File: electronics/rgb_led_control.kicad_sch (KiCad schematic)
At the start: 7 parts, among them J1 rgb_led_conn, Q3 N-MOS, Q4 N-MOS, Q5 N-MOS

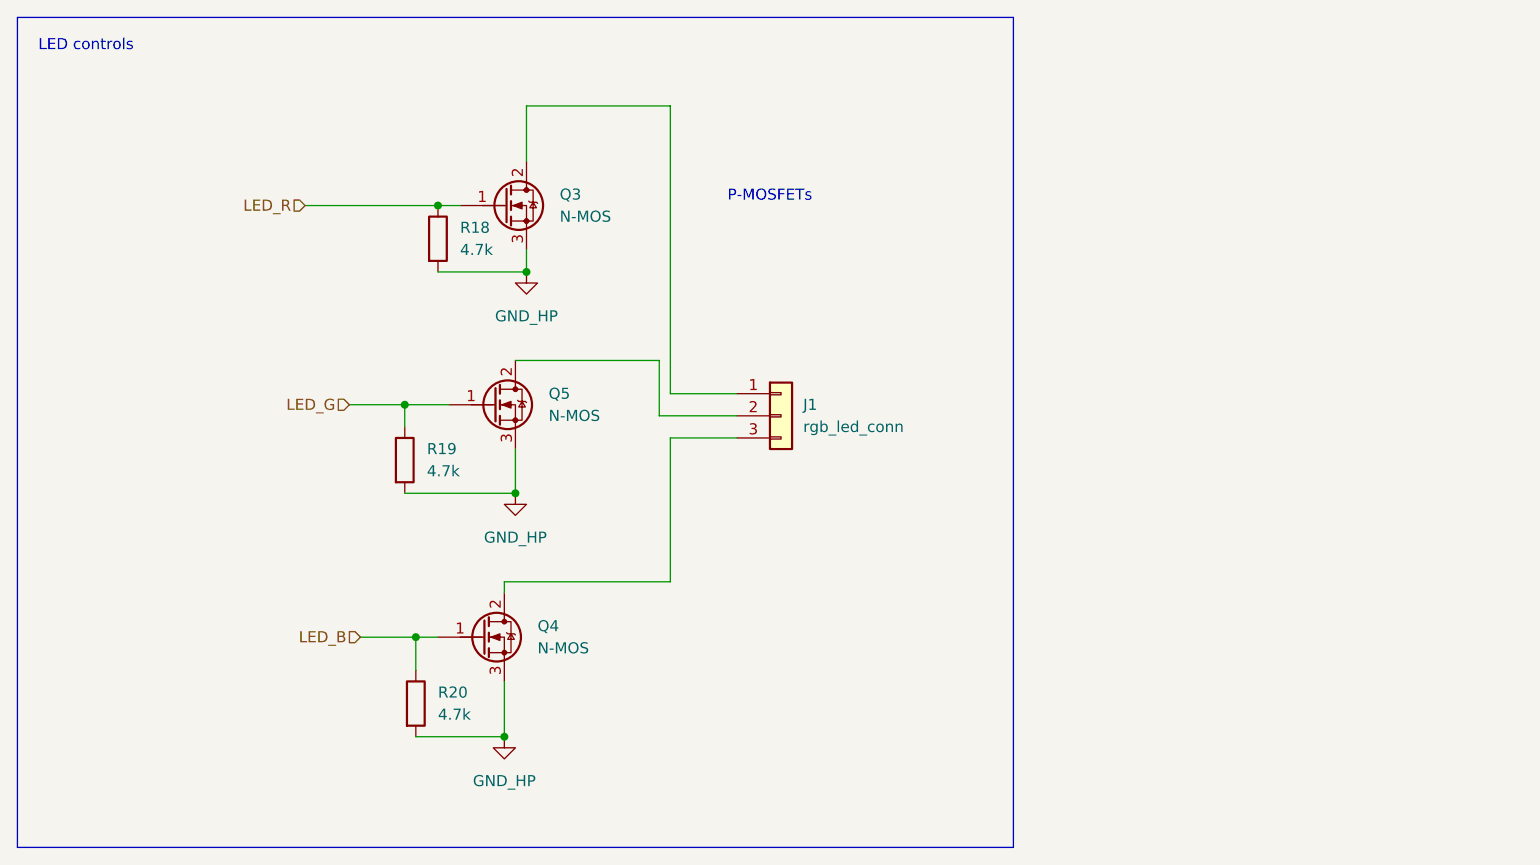
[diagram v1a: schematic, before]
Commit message: start to create BOM and finalising symbol fields
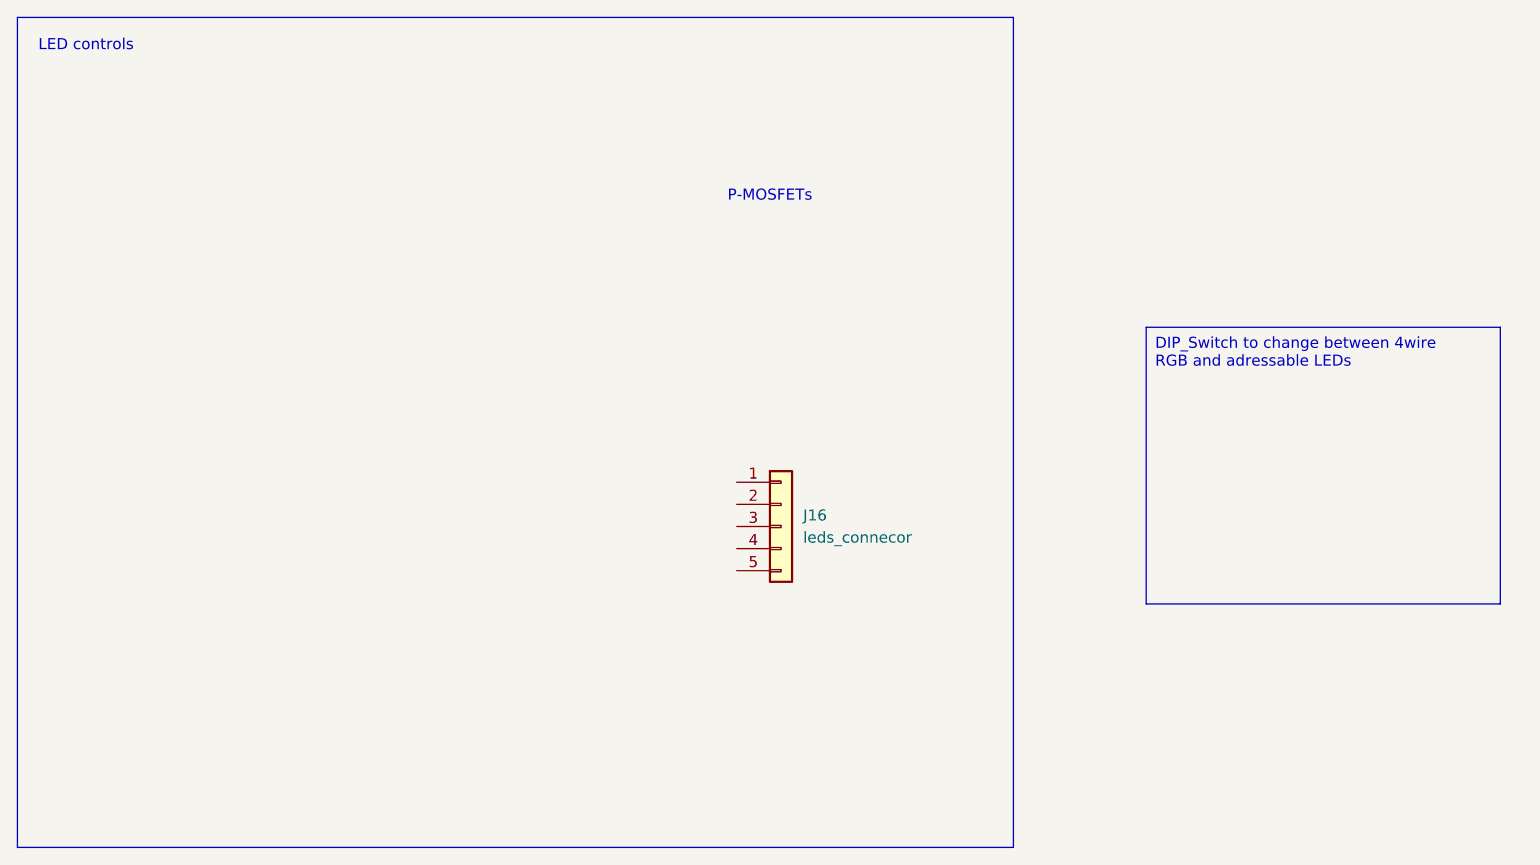
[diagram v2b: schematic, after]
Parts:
- removed J1: rgb_led_conn, TerminalBlock:TerminalBlock_Xinya_XY308-2.54-3P_1x03_P2.54mm_Horizontal, symbol Connector_Generic:Conn_01x03
- removed Q3, Q4, Q5: N-MOS, Package_TO_SOT_SMD:SOT-23, symbol Transistor_FET:BSP129
- removed R18, R19, R20: 4.7k, Resistor_SMD:R_0805_2012Metric_Pad1.20x1.40mm_HandSolder, symbol Device:R
- added J16: leds_connecor, TerminalBlock:TerminalBlock_Xinya_XY308-2.54-5P_1x05_P2.54mm_Horizontal, symbol Connector_Generic:Conn_01x05
